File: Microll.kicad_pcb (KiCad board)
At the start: 2 copper layers, 30 x 40 mm, 30 parts, among them J1 Conn_01x08, J2 Conn_01x08, J3 Conn_01x08, J4 USB_C_Receptacle, J5 Conn_01x08, U1 ESP32-C3-WROOM-02-N4, U2 TLV76733DRVx, U3 STM32G0B1CBU6, U4 USBLC6-2P6, U5 DPDT_Switch_x2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

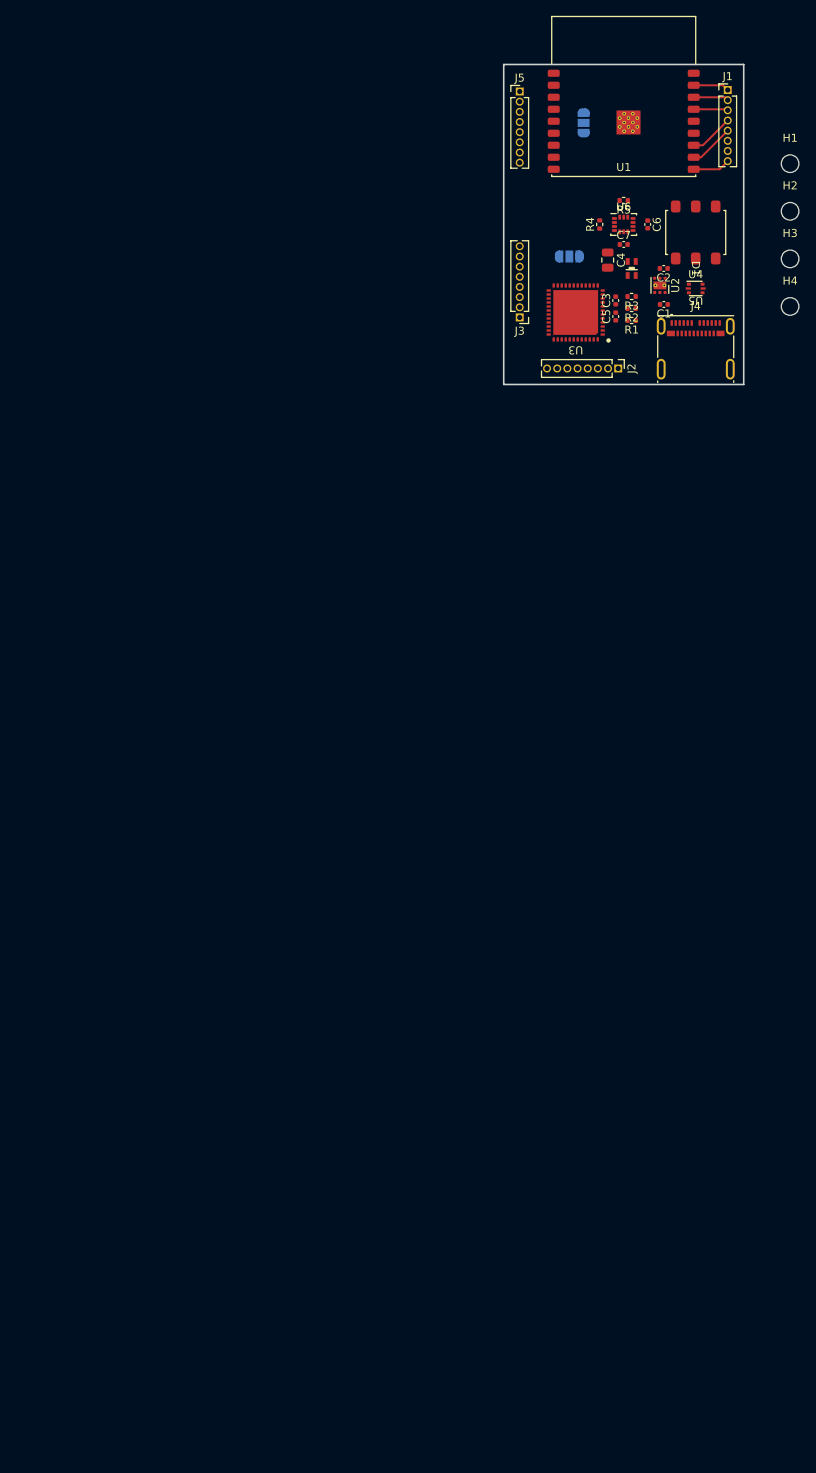
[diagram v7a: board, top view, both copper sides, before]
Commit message: Organised board sape and pin headers.
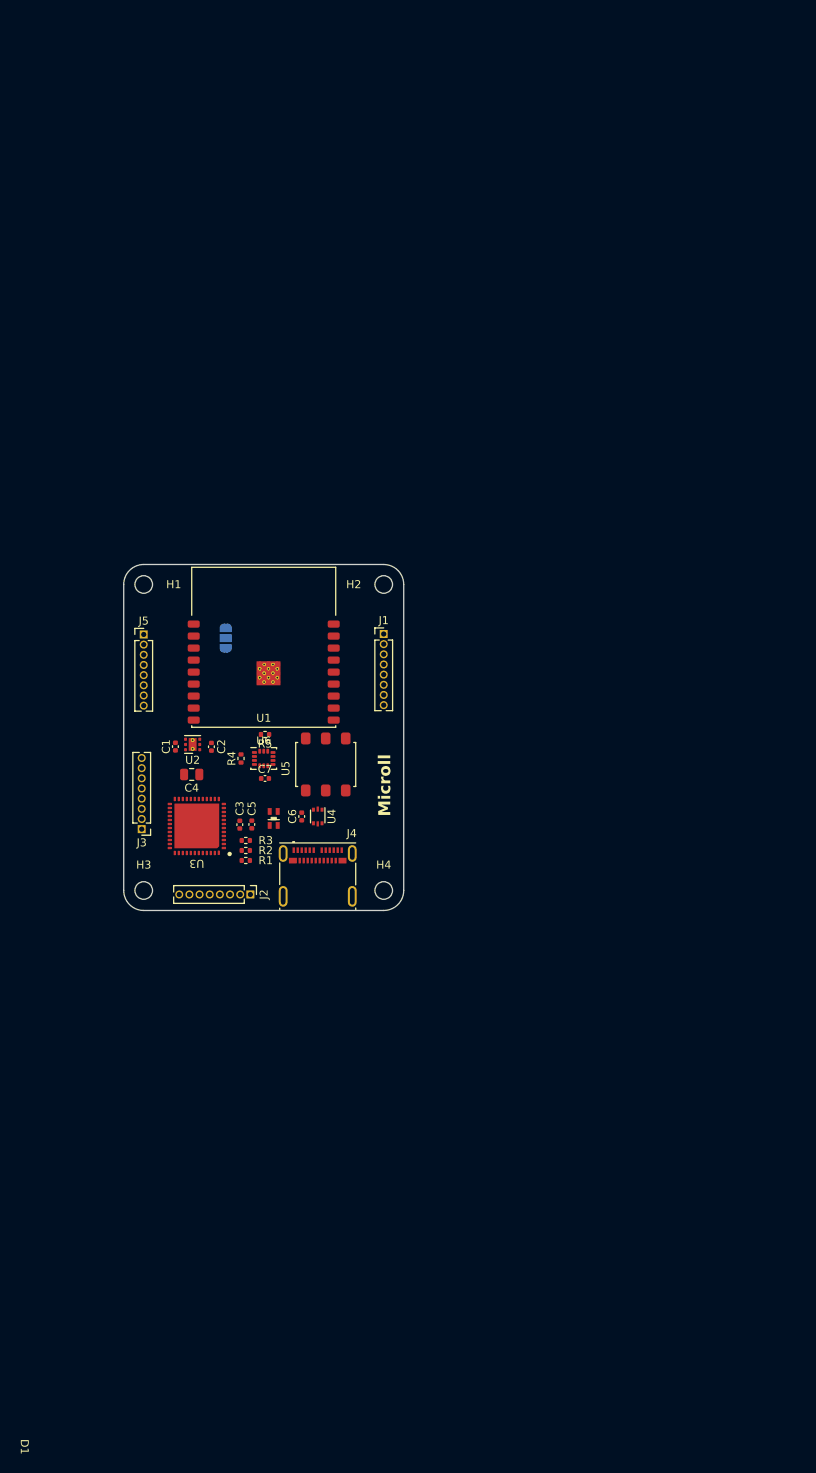
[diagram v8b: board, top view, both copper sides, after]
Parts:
- moved H3 113.0 mm to (105.0, 133.2)
- moved H1 96.4 mm to (105.0, 95.0)
- moved H4 88.9 mm to (135.0, 133.2)
- moved C6 85.7 mm to (124.8, 124.0), turned to 90 degrees
- moved JP2 85.1 mm to (111.8, 125.2)
- moved R3 83.4 mm to (117.8, 127.0)
- moved R2 83.2 mm to (117.8, 128.2)
- moved R1 83.0 mm to (117.8, 129.5)
- moved C4 82.7 mm to (111.0, 118.8), turned to 180 degrees
- moved J5 82.6 mm to (105.0, 101.2)
- moved C1 82.4 mm to (109.0, 115.3), turned to 90 degrees
- moved C2 82.3 mm to (113.5, 115.3), turned to 90 degrees
- moved U1 82.3 mm to (120.0, 106.0)
- moved D1 82.0 mm to (121.2, 124.2)
- moved U2 81.9 mm to (111.1, 115.0), turned to 180 degrees
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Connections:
- J2 pad 7: CAN_RX -> CAN_TX
- J2 pad 8: CAN_TX -> CAN_RX
- J3 pad 1: /ADC1_IN0 -> USART_RX
- J3 pad 2: /ADC1_IN1 -> USART_TX
- J3 pad 3: /PA8 -> /ADC1_IN0
- J3 pad 4: USART_RX -> /ADC1_IN1
- J3 pad 5: USART_TX -> /PA8
- J5 pad 1: SPI_MOSI -> /PA2
- J5 pad 2: SPI_MISO -> /PA3
- J5 pad 3: SPI_SCK -> /DAC1_OUT1
- J5 pad 4: /PA2 -> SPI_SCK
- J5 pad 5: /PA3 -> SPI_MISO
- J5 pad 6: /DAC1_OUT1 -> SPI_MOSI
- J5 pad 7: /PB1 -> /PB0
- J5 pad 8: /PB0 -> /PB1
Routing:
- net /Rx: track 5.63 -> 0.00 mm
- net /Tx: track 5.53 -> 0.00 mm
- net /GPIO10: track 4.67 -> 0.00 mm
- net /GPIO1: track 4.49 -> 0.00 mm
- net /GPIO2: track 4.40 -> 0.00 mm
- net /GPIO3: track 4.30 -> 0.00 mm
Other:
- board size 30 x 40 mm -> 35 x 43.2 mm
- board text added: "Microll"
